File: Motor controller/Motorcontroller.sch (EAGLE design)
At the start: 9 parts, among them IC1 L293D, IC2 7805TV

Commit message: Tested a motor
tested a motor under a power supply
roughly took 300mA to power 1 motor
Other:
- note added: "SINGLE MOTOR DRAW ~300mA UNDER POWER SUPPLY"
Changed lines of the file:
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@@
 <text x="45.72" y="81.28" size="1.778" layer="91">MOTOR CONTROL CIRCUIT</text>
 <text x="50.8" y="129.54" size="1.778" layer="91">5V REGULATOR</text>
+<text x="116.84" y="50.8" size="1.4224" layer="91">SINGLE MOTOR DRAW ~300mA
+UNDER POWER SUPPLY</text>
 </plain>
 <instances>
@@
 </drawing>
 <compatibility>
+<note version="6.3" minversion="6.2.2" severity="warning">
+Since Version 6.2.2 text objects can contain more than one line,
+which will not be processed correctly with this version.
+</note>
 <note version="8.2" severity="warning">
 Since Version 8.2, EAGLE supports online libraries. The ids

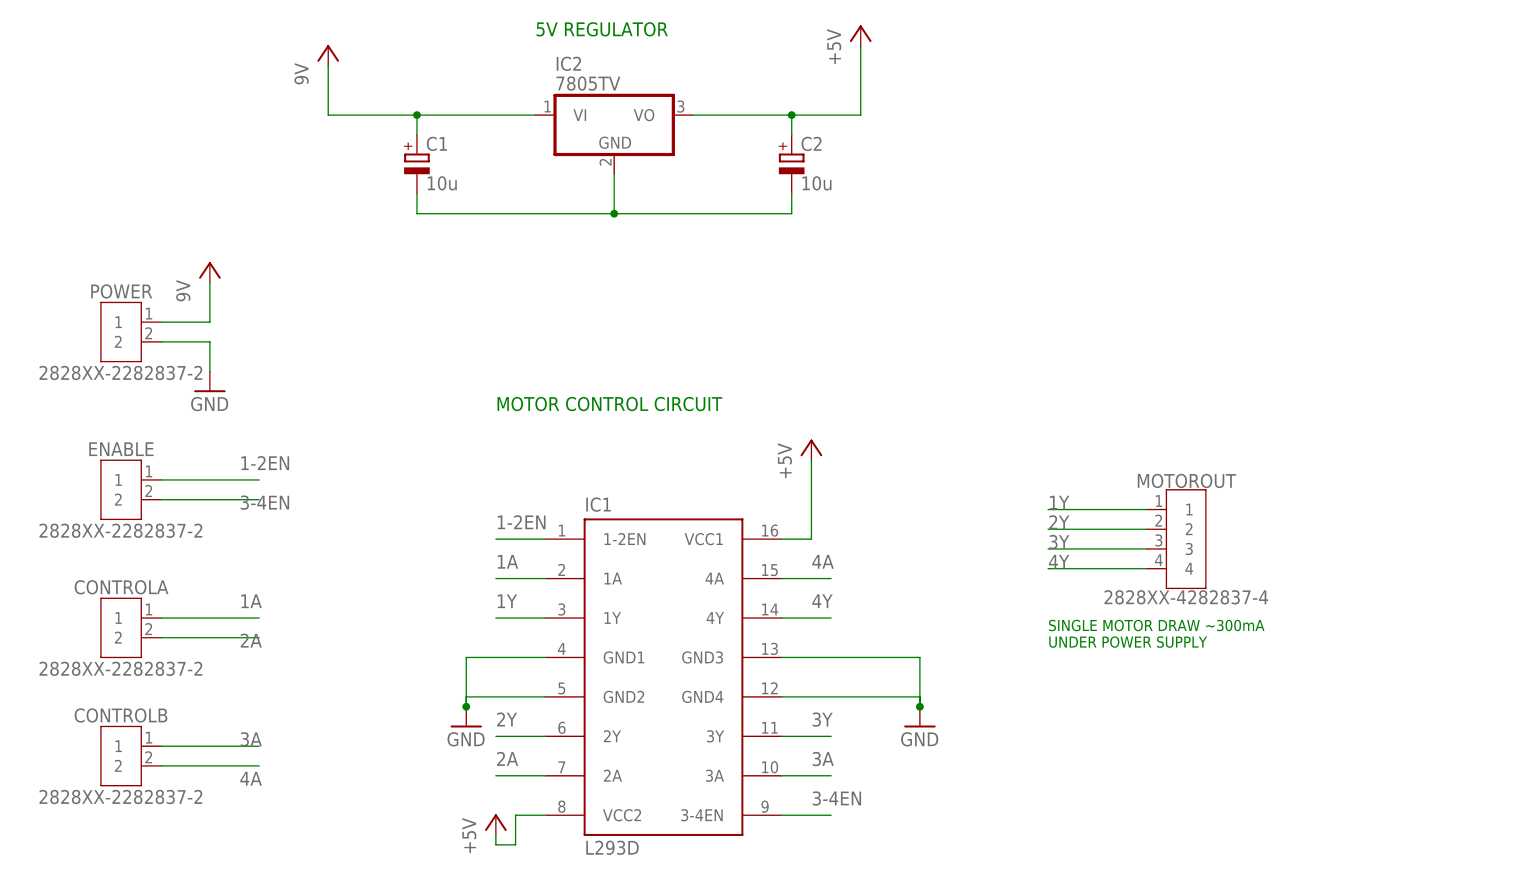
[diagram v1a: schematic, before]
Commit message: added protection diodes to circuit
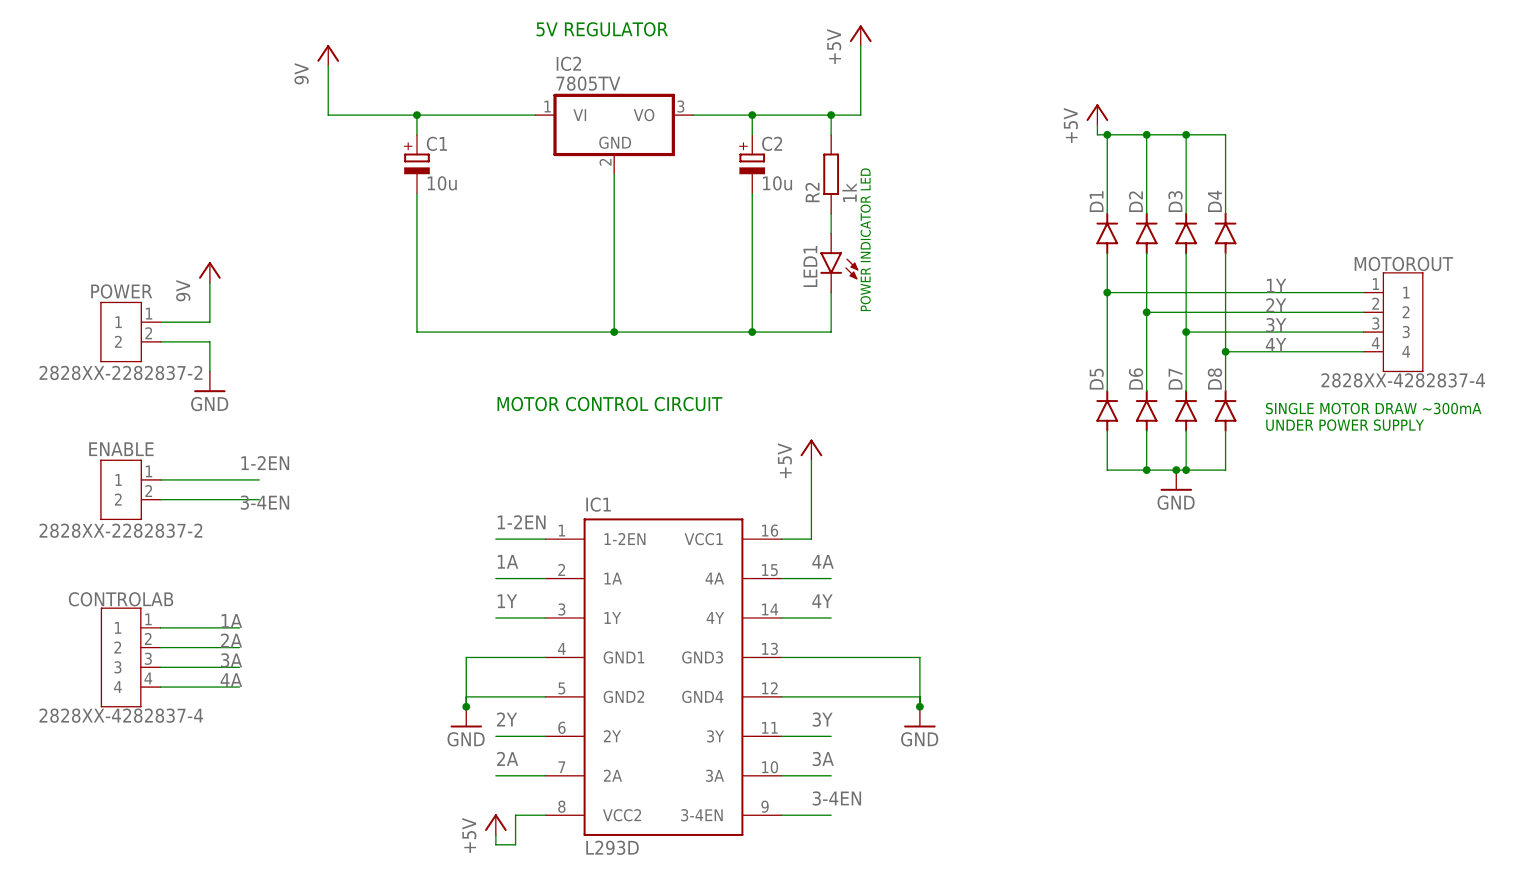
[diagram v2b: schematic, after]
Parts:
- removed CONTROLA, CONTROLB: 2828XX-2282837-2, Connector:2828XX-2282837-2
- added CONTROLAB: 2828XX-4282837-4, Connector:2828XX-4282837-4
- added D1, D2, D3, D4, D5, D6, D7, D8: (no value), diode:DIODE-DO214AC
- added LED1: (no value), led:LED5MM
- added R2: 1k, rcl:R-EU_R1206
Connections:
- new net N$2: LED1.A, R2.1
- net +5V: now also D1.C, D2.C, D3.C, D4.C, R2.2
- net 1A: now also CONTROLAB.1; no longer CONTROLA.1
- net 1Y: now also D1.A, D5.C
- net 2A: now also CONTROLAB.2; no longer CONTROLA.2
- net 2Y: now also D2.A, D6.C
- net 3A: now also CONTROLAB.3; no longer CONTROLB.1
- net 3Y: now also D3.A, D7.C
- net 4A: now also CONTROLAB.4; no longer CONTROLB.2
- net 4Y: now also D4.A, D8.C
- net GND: now also D5.A, D6.A, D7.A, D8.A
- net N$1: now also LED1.C
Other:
- note added: "POWER INDICATOR LED"
- moved on the sheet: C2, MOTOROUT
